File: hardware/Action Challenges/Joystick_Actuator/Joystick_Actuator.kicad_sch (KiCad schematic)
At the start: 4 parts, among them J1 ATTiny Prog, J2 Conn_01x04_Pin, U1 ATtiny1616-M

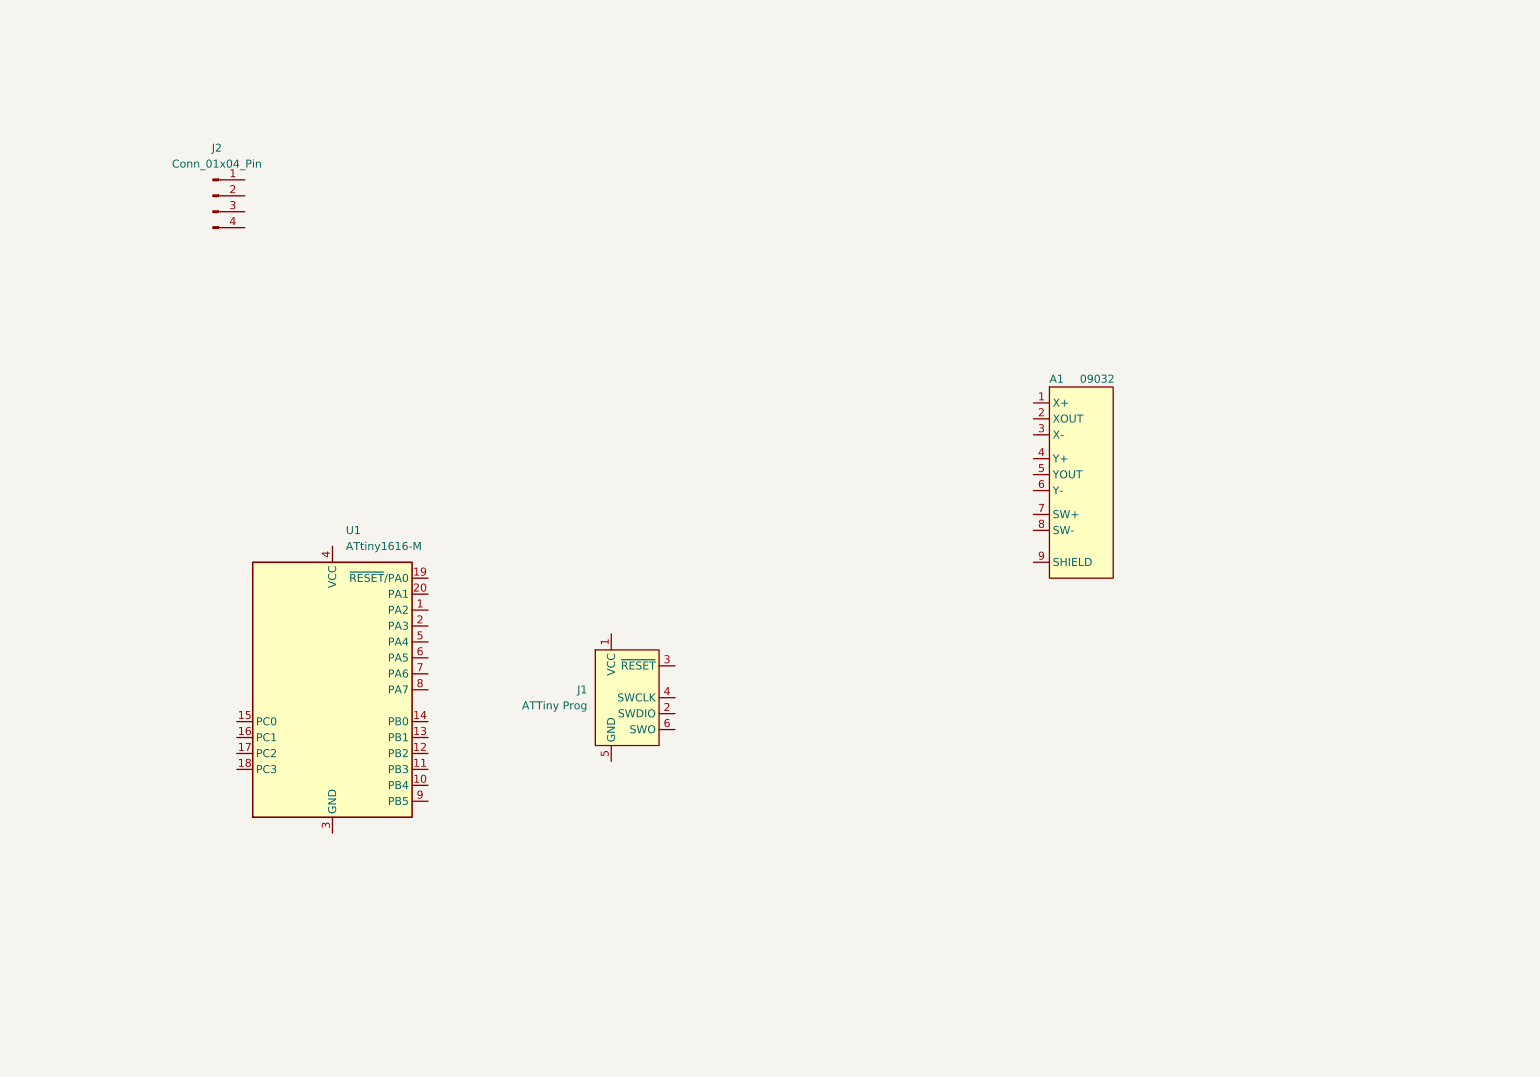
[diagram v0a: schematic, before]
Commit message: added major schematic components
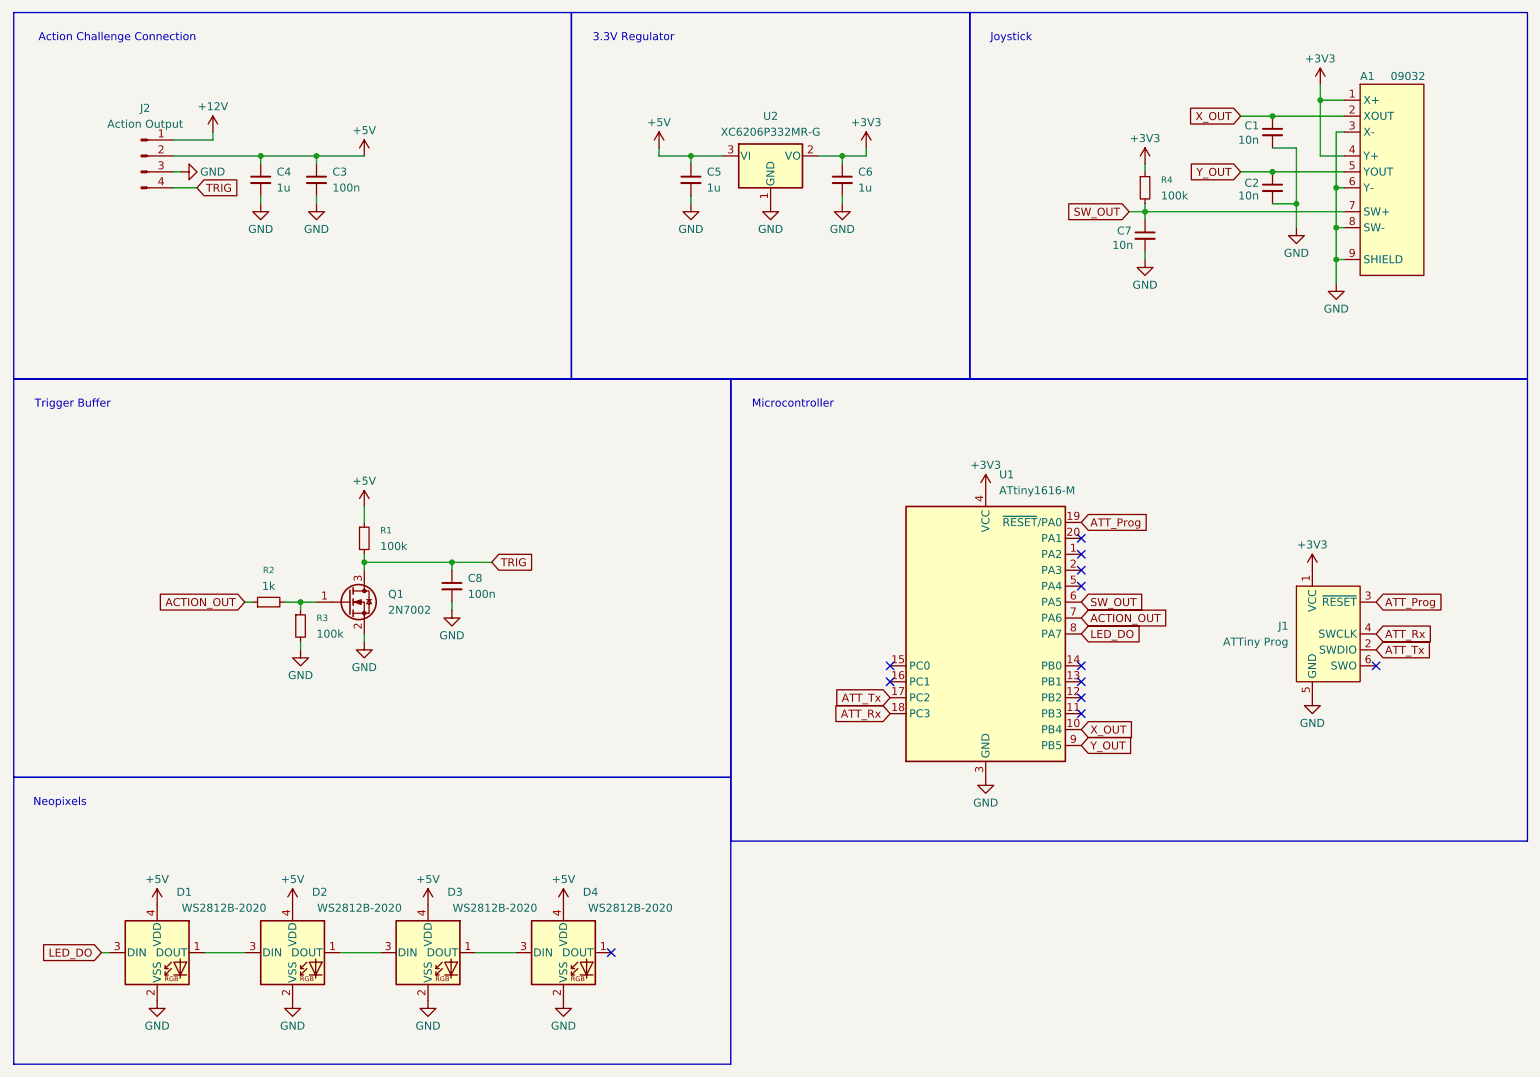
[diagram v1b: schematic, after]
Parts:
- added C1, C2, C7: 10n, Capacitor_SMD:C_0402_1005Metric, symbol Device:C_Small
- added C3, C8: 100n, Capacitor_SMD:C_0402_1005Metric, symbol Device:C_Small
- added C4, C5, C6: 1u, Capacitor_SMD:C_0402_1005Metric, symbol Device:C_Small
- added D1, D2, D3, D4: WS2812B-2020, LED_SMD:LED_WS2812B-2020_PLCC4_2.0x2.0mm, symbol LED:WS2812B-2020
- added Q1: 2N7002, Package_TO_SOT_SMD:SOT-23, symbol Transistor_FET:2N7002
- added R1, R3, R4: 100k, Resistor_SMD:R_0402_1005Metric, symbol Device:R_Small
- added R2: 1k, Resistor_SMD:R_0402_1005Metric, symbol Device:R_Small
- added U2: XC6206P332MR-G, Package_TO_SOT_SMD:SOT-23-3, symbol Regulator_Linear:XC6206PxxxMR
- J2: value Conn_01x04_Pin -> Action Output; footprint (none) -> Connector_JST:JST_XH_S4B-XH-A_1x04_P2.50mm_Horizontal
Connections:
- net +3V3: now reaches A1.1 (X+)
- net +3V3: now also A1.4 (Y+), J1.1 (VCC), U1.4 (VCC), C6.1, R4.1, U2.2 (VO)
- net X_OUT: now reaches A1.2 (XOUT)
- net X_OUT: now also U1.10 (PB4), C1.1
- net GND: now reaches A1.3 (X-)
- net GND: now also A1.6 (Y-), A1.8 (SW-), A1.9 (SHIELD), J1.5 (GND), J2.3 (Pin_3), U1.21 (GND), U1.3 (GND), C1.2, C2.2, C3.2, C4.2, C5.2, C6.2, C7.2, C8.2, D1.2 (VSS), D2.2 (VSS), D3.2 (VSS), D4.2 (VSS), Q1.2 (S), R3.2, U2.1 (GND)
- net Y_OUT: now reaches A1.5 (YOUT)
- net Y_OUT: now also U1.9 (PB5), C2.1
- net SW_OUT: now reaches A1.7 (SW+)
- net SW_OUT: now also U1.6 (PA5), C7.1, R4.2
- net ATT_Tx: now reaches J1.2 (SWDIO)
- net ATT_Tx: now also U1.17 (PC2)
- net ATT_Prog: now reaches J1.3 (~{RESET})
- net ATT_Prog: now also U1.19 (~{RESET}/PA0)
- net ATT_Rx: now reaches J1.4 (SWCLK)
- net ATT_Rx: now also U1.18 (PC3)
- net ACTION_OUT: now reaches U1.7 (PA6)
- net ACTION_OUT: now also R2.1
- net LED_DO: now reaches U1.8 (PA7)
- net LED_DO: now also D1.3 (DIN)
- net +12V: now reaches J2.1 (Pin_1)
- net +5V: now reaches J2.2 (Pin_2)
- net +5V: now also C3.1, C4.1, C5.1, D1.4 (VDD), D2.4 (VDD), D3.4 (VDD), D4.4 (VDD), R1.1, U2.3 (VI)
- net TRIG: now reaches J2.4 (Pin_4)
- net TRIG: now also C8.1, Q1.3 (D), R1.2
- new net: Q1.1 (G), R2.2, R3.1
- new net: D1.1 (DOUT), D2.3 (DIN)
- new net: D2.1 (DOUT), D3.3 (DIN)
- new net: D3.1 (DOUT), D4.3 (DIN)
- no-connect marks 0 -> 12
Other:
- note added: "3.3V Regulator"
- note added: "Action Challenge Connection"
- note added: "Joystick"
- note added: "Microcontroller"
- note added: "Neopixels"
- note added: "Trigger Buffer"
- moved on the sheet: A1, J1, J2, U1

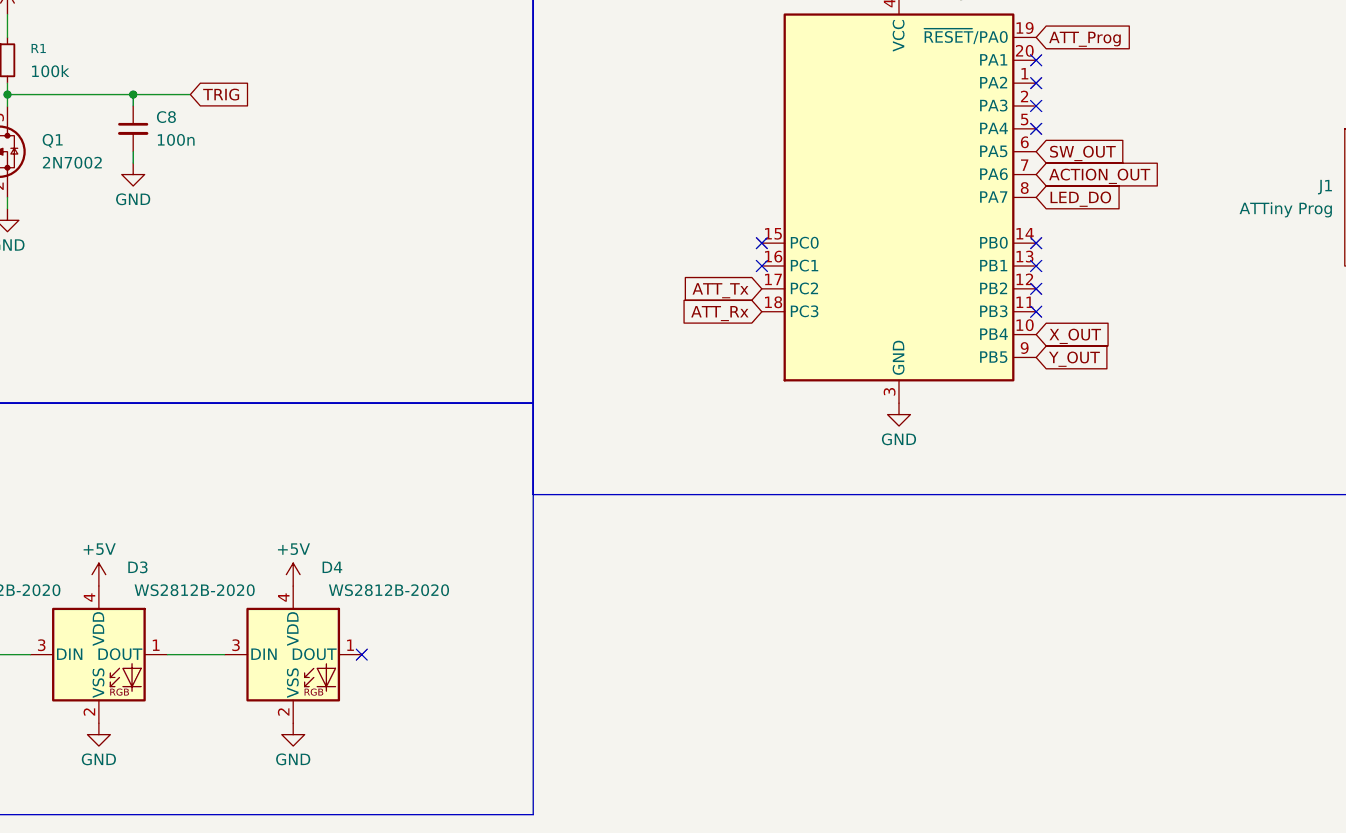
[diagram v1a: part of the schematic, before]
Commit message: placed components and added power/signal traces
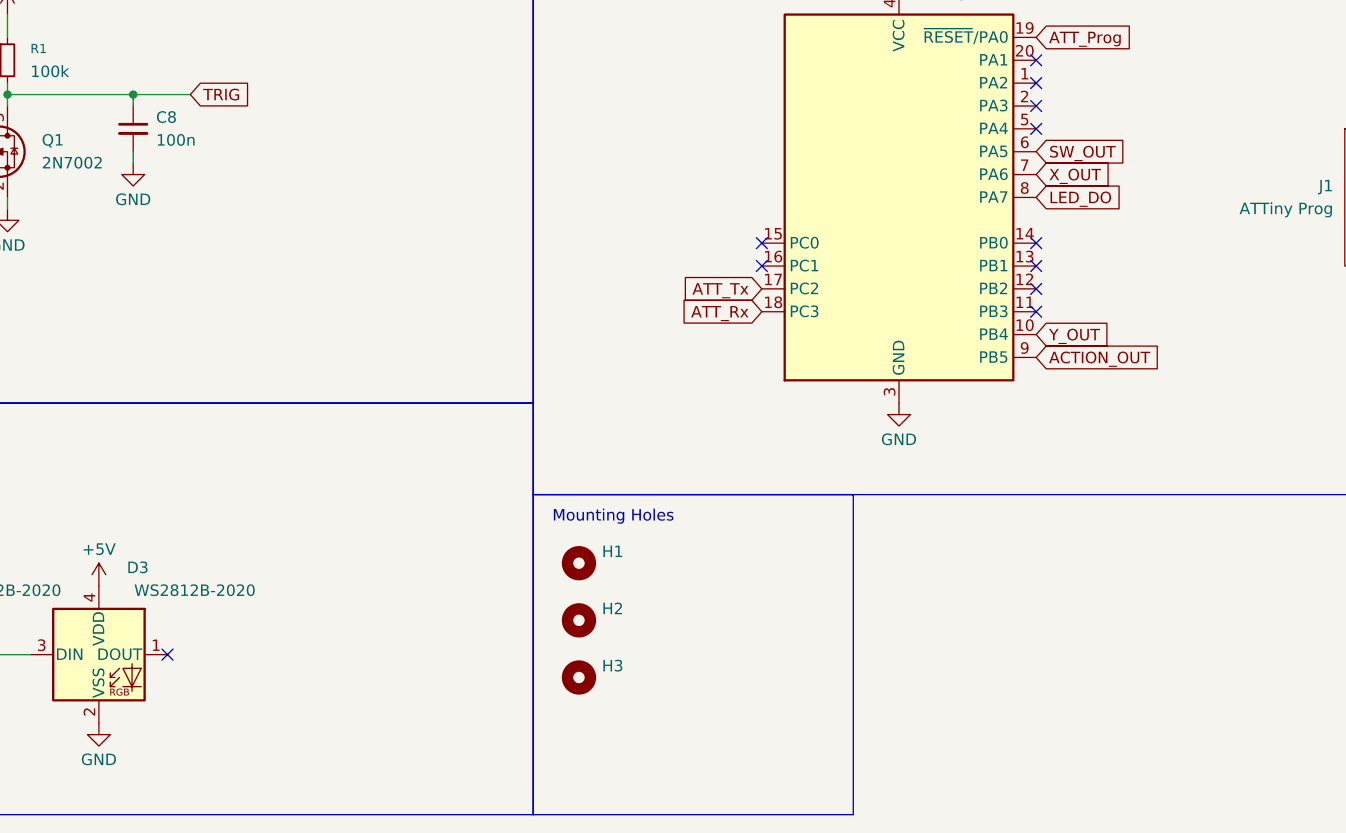
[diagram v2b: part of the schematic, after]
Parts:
- removed D4: WS2812B-2020, LED_SMD:LED_WS2812B-2020_PLCC4_2.0x2.0mm, symbol LED:WS2812B-2020
- added H1, H2, H3: MountingHole, MountingHole:MountingHole_3.5mm, symbol Mechanical:MountingHole
- D1, D2, D3: MPN (none) -> C965555
- J1: footprint Connector:Tag-Connect_TC2030-IDC-FP_2x03_P1.27mm_Vertical -> Connector:Tag-Connect_TC2030-IDC-NL_2x03_P1.27mm_Vertical
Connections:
- net ACTION_OUT: now also U1.9 (PB5); no longer U1.7 (PA6)
- net X_OUT: now also U1.7 (PA6); no longer U1.10 (PB4)
- net Y_OUT: now also U1.10 (PB4); no longer U1.9 (PB5)
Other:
- note added: "Mounting Holes"

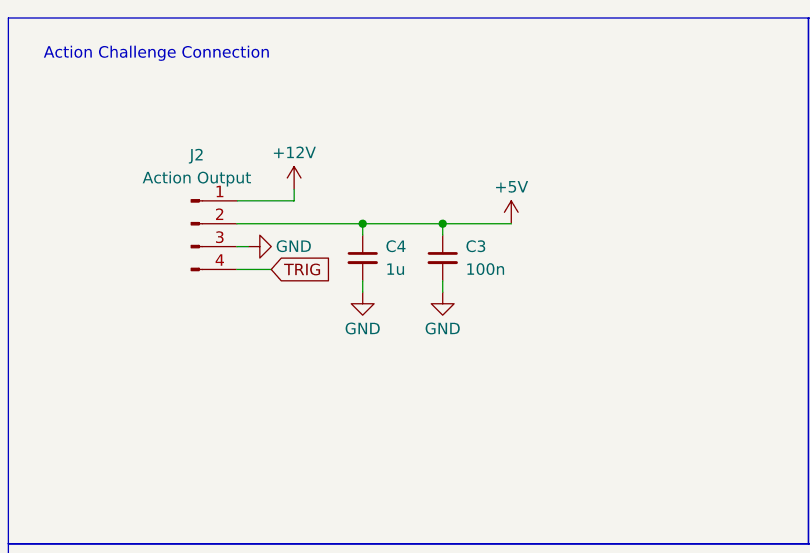
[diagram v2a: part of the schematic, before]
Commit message: Added remaining routing and MPNs
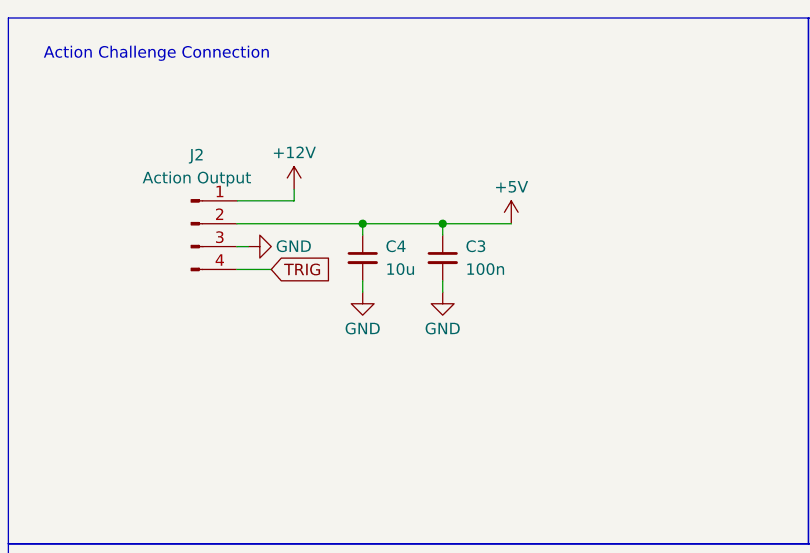
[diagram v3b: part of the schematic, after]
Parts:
- C1, C2, C7: MPN C15195 -> C15195
- C3, C8: MPN (none) -> C1525
- C4: value 1u -> 10u; footprint Capacitor_SMD:C_0402_1005Metric -> Capacitor_SMD:C_0603_1608Metric; MPN (none) -> C19702
- C5, C6: MPN (none) -> C52923
- U1: MPN (none) -> C507118
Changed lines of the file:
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@@
 			)
 		)
-		(property "MPN" " C15195"
+		(property "MPN" "C15195"
 			(at 223.52 48.26 0)
 			(hide yes)
@@
 			)
 		)
-		(property "MPN" " C15195"
+		(property "MPN" "C15195"
 			(at 223.52 39.37 0)
 			(hide yes)
@@
 			)
 		)
+		(property "MPN" "C1525"
+			(at 92.71 111.76 0)
+			(hide yes)
+			(show_name no)
+			(do_not_autoplace no)
+			(effects
+				(font
+					(size 1.27 1.27)
+				)
+			)
+		)
 		(pin "2"
 		)
@@
 			)
 		)
+		(property "MPN" "C52923"
+			(at 130.81 46.99 0)
+			(hide yes)
+			(show_name no)
+			(do_not_autoplace no)
+			(effects
+				(font
+					(size 1.27 1.27)
+				)
+			)
+		)
 		(pin "2"
 		)
@@
 			)
 		)
+		(property "MPN" "C1525"
+			(at 71.12 46.99 0)
+			(hide yes)
+			(show_name no)
+			(do_not_autoplace no)
+			(effects
+				(font
+					(size 1.27 1.27)
+				)
+			)
+		)
 		(pin "2"
 		)
@@
 			)
 		)
+		(property "MPN" "C52923"
+			(at 154.94 46.99 0)
+			(hide yes)
+			(show_name no)
+			(do_not_autoplace no)
+			(effects
+				(font
+					(size 1.27 1.27)
+				)
+			)
+		)
 		(pin "2"
 		)
@@
 			)
 		)
-		(property "MPN" " C15195"
+		(property "MPN" "C15195"
 			(at 203.2 55.88 0)
 			(hide yes)
@@
 			)
 		)
-		(property "Value" "1u"
+		(property "Value" "10u"
 			(at 64.77 48.2662 0)
 			(show_name no)
@@
 			)
 		)
-		(property "Footprint" "Capacitor_SMD:C_0402_1005Metric"
+		(property "Footprint" "Capacitor_SMD:C_0603_1608Metric"
 			(at 62.23 46.99 0)
 			(hide yes)
@@
 			)
 		)
+		(property "MPN" "C19702"
+			(at 62.23 46.99 0)
+			(hide yes)
+			(show_name no)
+			(do_not_autoplace no)
+			(effects
+				(font
+					(size 1.27 1.27)
+				)
+			)
+		)
 		(pin "2"
 		)
@@
 			(at 177.8 119.38 0)
 			(hide yes)
+			(show_name no)
+			(do_not_autoplace no)
+			(effects
+				(font
+					(size 1.27 1.27)
+				)
+			)
+		)
+		(property "MPN" "C507118"
+			(at 177.8 119.38 0)
+			(hide yes)
